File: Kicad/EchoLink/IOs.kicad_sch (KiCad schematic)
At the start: 5 parts, among them J3 Conn_01x08_Pin, J4 Conn_01x06_Pin, J5 Conn_01x09_Socket

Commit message: wip: add comments in schematic
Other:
- note added: "*IMPORTANT STLinkV2 fourni seulement 100-250mA Debogguer avec alimentation 3v3/5v externe"
- moved on the sheet: D2, R15
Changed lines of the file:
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@@
 	(rectangle
 		(start 15.24 85.09)
-		(end 59.69 111.76)
+		(end 61.595 118.745)
 		(stroke
 			(width 0)
@@
 		)
 	)
+	(text "*IMPORTANT\nSTLinkV2 fourni seulement 100-250mA\nDebogguer avec alimentation 3v3/5v externe"
+		(exclude_from_sim no)
+		(at 15.494 115.57 0)
+		(effects
+			(font
+				(size 1.27 1.27)
+				(thickness 0.254)
+				(bold yes)
+				(italic yes)
+			)
+			(justify left)
+		)
+	)
 	(text "HAL_LPTIM_PWM_Start(&hlptim2, 31999, 28799)\nPériode 1s / Flash 100ms\nILED = (3.3 - 2.1) / 1500 = 0.8mA"
 		(exclude_from_sim no)
@@
 	(wire
 		(pts
-			(xy 44.45 71.12) (xy 45.72 71.12)
+			(xy 48.26 71.12) (xy 49.53 71.12)
 		)
 		(stroke
@@
 	(wire
 		(pts
-			(xy 54.61 71.12) (xy 54.61 72.39)
+			(xy 58.42 71.12) (xy 58.42 72.39)
 		)
 		(stroke
@@
 	(wire
 		(pts
-			(xy 35.56 71.12) (xy 36.83 71.12)
-		)
-		(stroke
-			(width 0)
-			(type default)
-		)
-	)
-	(wire
-		(pts
-			(xy 53.34 71.12) (xy 54.61 71.12)
+			(xy 39.37 71.12) (xy 40.64 71.12)
+		)
+		(stroke
+			(width 0)
+			(type default)
+		)
+	)
+	(wire
+		(pts
+			(xy 57.15 71.12) (xy 58.42 71.12)
 		)
 		(stroke
@@
 	(global_label "PWR_LPTIM2_OUT"
 		(shape input)
-		(at 35.56 71.12 180)
+		(at 39.37 71.12 180)
 		(fields_autoplaced yes)
 		(effects
@@
 		)
 		(property "Intersheetrefs" "${INTERSHEET_REFS}"
-			(at 16.4882 71.12 0)
+			(at 20.2982 71.12 0)
 			(hide yes)
 			(show_name no)
@@
 	(symbol
 		(lib_id "Device:LED")
-		(at 49.53 71.12 180)
+		(at 53.34 71.12 180)
 		(unit 1)
 		(body_style 1)
@@
 		(dnp no)
 		(property "Reference" "D2"
-			(at 48.514 68.834 0)
+			(at 52.324 68.834 0)
 			(show_name no)
 			(do_not_autoplace no)
@@
 		)
 		(property "Value" "GREEN"
-			(at 46.99 73.66 0)
+			(at 50.8 73.66 0)
 			(show_name no)
 			(do_not_autoplace no)
@@
 		)
 		(property "Footprint" "ODB:LED_QBLP601-AG15"
-			(at 49.53 71.12 0)
+			(at 53.34 71.12 0)
 			(hide yes)
 			(show_name no)
@@
 		)
 		(property "Datasheet" "https://www.digikey.ca/en/products/detail/qt-brightek-qtb/QBLP601-AG15/16499667"
-			(at 49.53 71.12 0)
+			(at 53.34 71.12 0)
 			(hide yes)
 			(show_name no)
@@
 		)
 		(property "Description" ""
-			(at 49.53 71.12 0)
+			(at 53.34 71.12 0)
 			(hide yes)
 			(show_name no)
@@
 		)
 		(property "DigiKey_Part_Number" "1516-QBLP601-AG15CT-ND"
-			(at 49.53 71.12 0)
+			(at 53.34 71.12 0)
 			(hide yes)
 			(show_name no)
@@
 		)
 		(property "Purchase-URL" ""
-			(at 49.53 71.12 0)
+			(at 53.34 71.12 0)
 			(hide yes)
 			(show_name no)
@@
 		)
 		(property "Sim.Device" ""
-			(at 49.53 71.12 0)
+			(at 53.34 71.12 0)
 			(hide yes)
 			(show_name no)
@@
 		)
 		(property "Sim.Pins" ""
-			(at 49.53 71.12 0)
+			(at 53.34 71.12 0)
 			(hide yes)
 			(show_name no)
@@
 		)
 		(property "Sim.Type" ""
-			(at 49.53 71.12 0)
+			(at 53.34 71.12 0)
 			(hide yes)
 			(show_name no)
@@
 		)
 		(property "Manufacturer_Part_Number" "QBLP601-AG15"
-			(at 49.53 71.12 0)
+			(at 53.34 71.12 0)
 			(hide yes)
 			(show_name no)
@@
 	(symbol
 		(lib_id "power:GND")
-		(at 54.61 72.39 0)
+		(at 58.42 72.39 0)
 		(unit 1)
 		(body_style 1)
@@
 		(fields_autoplaced yes)
 		(property "Reference" "#PWR045"
-			(at 54.61 78.74 0)
+			(at 58.42 78.74 0)
 			(hide yes)
 			(show_name no)
@@
 		)
 		(property "Value" "GND"
-			(at 54.61 77.47 0)
+			(at 58.42 77.47 0)
 			(hide yes)
 			(show_name no)
@@
 		)
 		(property "Footprint" ""
-			(at 54.61 72.39 0)
+			(at 58.42 72.39 0)
 			(hide yes)
 			(show_name no)
@@
 		)
 		(property "Datasheet" ""
-			(at 54.61 72.39 0)
+			(at 58.42 72.39 0)
 			(hide yes)
 			(show_name no)
@@
 		)
 		(property "Description" ""
-			(at 54.61 72.39 0)
+			(at 58.42 72.39 0)
 			(hide yes)
 			(show_name no)
@@
 	(symbol
 		(lib_id "Device:R")
-		(at 40.64 71.12 90)
+		(at 44.45 71.12 90)
 		(unit 1)
 		(body_style 1)
@@
 		(dnp no)
 		(property "Reference" "R15"
-			(at 39.624 69.088 90)
+			(at 43.434 69.088 90)
 			(show_name no)
 			(do_not_autoplace no)
@@
 		)
 		(property "Value" "1.5k"
-			(at 44.45 69.088 90)
+			(at 48.26 69.088 90)
 			(show_name no)
 			(do_not_autoplace no)
@@
 		)
 		(property "Footprint" "Resistor_SMD:R_0603_1608Metric"
-			(at 40.64 72.898 90)
+			(at 44.45 72.898 90)
 			(hide yes)
 			(show_name no)
@@
 		)
 		(property "Datasheet" "https://www.digikey.ca/en/products/detail/panasonic-electronic-components/ERA-3AEB152V/1465858"
-			(at 40.64 71.12 0)
+			(at 44.45 71.12 0)
 			(hide yes)
 			(show_name no)
@@
 		)
 		(property "Description" "Resistor"
-			(at 40.64 71.12 0)
+			(at 44.45 71.12 0)
 			(hide yes)
 			(show_name no)
@@
 		)
 		(property "DigiKey_Part_Number" "P1.5KDBCT-ND"
-			(at 40.64 71.12 90)
+			(at 44.45 71.12 90)
 			(hide yes)
 			(show_name no)
@@
 		)
 		(property "Purchase-URL" ""
-			(at 40.64 71.12 90)
+			(at 44.45 71.12 90)
 			(hide yes)
 			(show_name no)
@@
 		)
 		(property "Sim.Device" ""
-			(at 40.64 71.12 90)
+			(at 44.45 71.12 90)
 			(hide yes)
 			(show_name no)
@@
 		)
 		(property "Sim.Pins" ""
-			(at 40.64 71.12 90)
+			(at 44.45 71.12 90)
 			(hide yes)
 			(show_name no)
@@
 		)
 		(property "Sim.Type" ""
-			(at 40.64 71.12 90)
+			(at 44.45 71.12 90)
 			(hide yes)
 			(show_name no)
@@
 		)
 		(property "Manufacturer_Part_Number" "ERA-3AEB152V"
-			(at 40.64 71.12 90)
-			(hide yes)
-			(show_name no)
+			(at 44.45 71.12 90)
+			(hide yes)
+			(show_name no)

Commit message: wip: add 470uF cap to lora module decoupling capacitance
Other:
- note added: "*Torsader VCC/GND*"
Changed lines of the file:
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@@
+		)
+	)
+	(text "*Torsader VCC/GND*"
+		(exclude_from_sim no)
+		(at 44.45 36.068 0)
+		(effects
+			(font
+				(size 1.27 1.27)
+				(thickness 0.254)
+				(bold yes)
+				(italic yes)
+			)
+			(justify left)
 		)
 	)

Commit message: wip: rename compoents
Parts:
- D2: footprint ODB:LED_QBLP601-AG15 -> (none)
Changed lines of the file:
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@@
 			)
 		)
-		(property "Footprint" "ODB:LED_QBLP601-AG15"
+		(property "Footprint" ""
 			(at 53.34 71.12 0)
 			(hide yes)

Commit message: wip: connector and bms IOs
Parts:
- removed J3: Conn_01x08_Pin, symbol Connector:Conn_01x08_Pin
- removed J5: Conn_01x09_Socket, symbol Connector:Conn_01x09_Socket
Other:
- moved on the sheet: D2, J4, R15

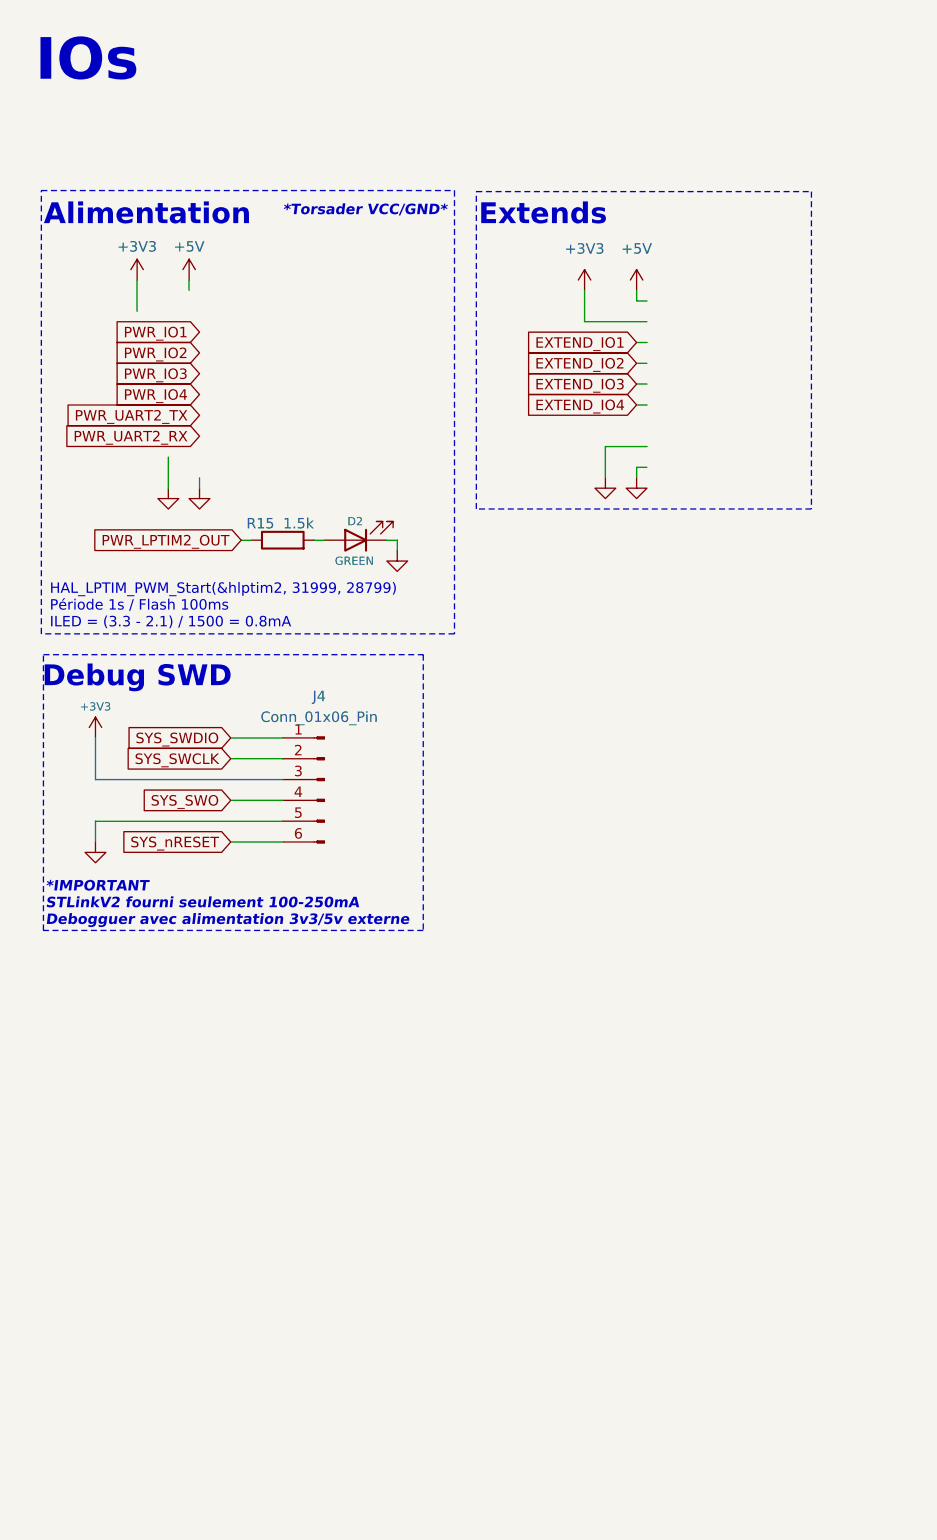
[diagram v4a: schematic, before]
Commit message: fix: rework all schematics to fit with new design and update stm32cubemx project
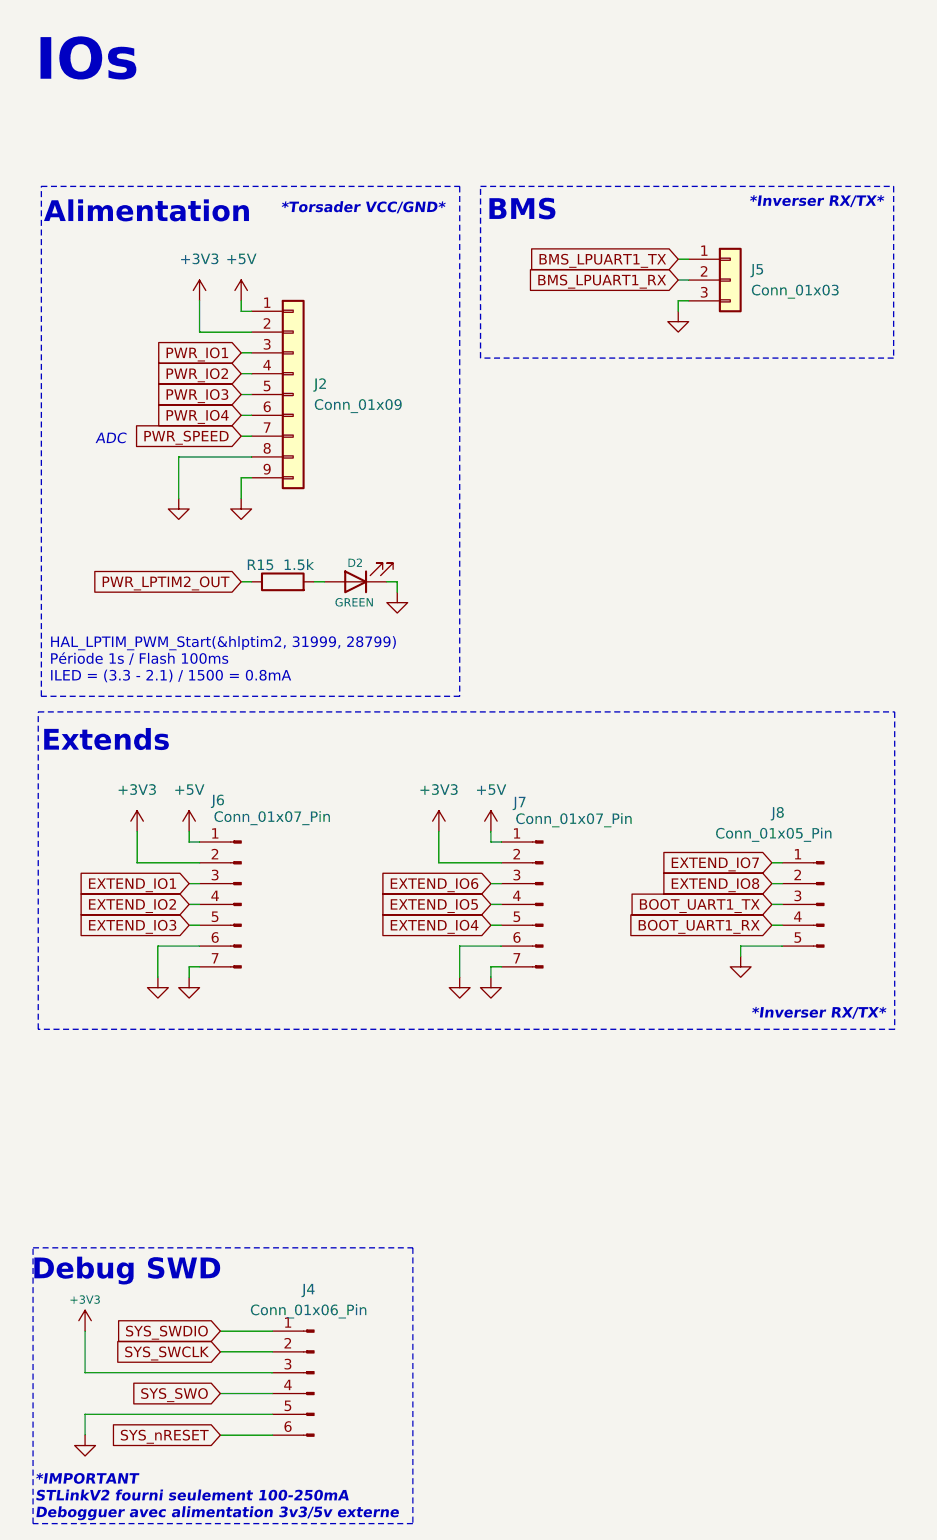
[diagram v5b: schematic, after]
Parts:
- added J2: Conn_01x09, symbol Connector_Generic:Conn_01x09
- added J5: Conn_01x03, Connector_RJ:RJ45_Abracon_ARJP11A-MA_Horizontal, symbol Connector_Generic:Conn_01x03
- added J6, J7: Conn_01x07_Pin, symbol Connector:Conn_01x07_Pin
- added J8: Conn_01x05_Pin, symbol Connector:Conn_01x05_Pin
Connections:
- net +3V3: now also J2.2 (Pin_2), J6.2 (Pin_2), J7.2 (Pin_2)
- net +5V: now also J2.1 (Pin_1), J6.1 (Pin_1), J7.1 (Pin_1)
- net EXTEND_IO1: now also J6.3 (Pin_3)
- net EXTEND_IO2: now also J6.4 (Pin_4)
- net EXTEND_IO3: now also J6.5 (Pin_5)
- net EXTEND_IO4: now also J7.5 (Pin_5)
- net GND: now also J2.8 (Pin_8), J2.9 (Pin_9), J5.3 (Pin_3), J6.6 (Pin_6), J6.7 (Pin_7), J7.6 (Pin_6), J7.7 (Pin_7), J8.5 (Pin_5)
- net PWR_IO1: now also J2.3 (Pin_3)
- net PWR_IO2: now also J2.4 (Pin_4)
- net PWR_IO3: now also J2.5 (Pin_5)
- net PWR_IO4: now also J2.6 (Pin_6)
- new net BMS_LPUART1_RX: J5.2 (Pin_2)
- new net BMS_LPUART1_TX: J5.1 (Pin_1)
- new net BOOT_UART1_RX: J8.4 (Pin_4)
- new net BOOT_UART1_TX: J8.3 (Pin_3)
- new net EXTEND_IO5: J7.4 (Pin_4)
- new net EXTEND_IO6: J7.3 (Pin_3)
- new net EXTEND_IO7: J8.1 (Pin_1)
- new net EXTEND_IO8: J8.2 (Pin_2)
- new net PWR_SPEED: J2.7 (Pin_7)
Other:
- note added: "*Inverser RX/TX*"
- note added: "ADC"
- note added: "BMS"
- moved on the sheet: D2, J4, R15

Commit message: wip: add missing footprints
- connectors missing
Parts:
- D2: footprint (none) -> Resistor_SMD:R_0603_1608Metric
- J3: renamed from J6; footprint (none) -> Connector_PinHeader_2.54mm:PinHeader_1x07_P2.54mm_Vertical
- J5: renamed from J7; footprint (none) -> Connector_PinHeader_2.54mm:PinHeader_1x07_P2.54mm_Vertical
- J6: renamed from J5; footprint Connector_RJ:RJ45_Abracon_ARJP11A-MA_Horizontal -> (none)
- J8: footprint (none) -> Connector_PinHeader_2.54mm:PinHeader_1x05_P2.54mm_Vertical
- renumbered J2 to J4, J4 to J7, R15 to R17
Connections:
- net BOOT_UART1_RX renamed EXTEND_UART1_RX
- net BOOT_UART1_TX renamed EXTEND_UART1_TX
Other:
- moved on the sheet: J7

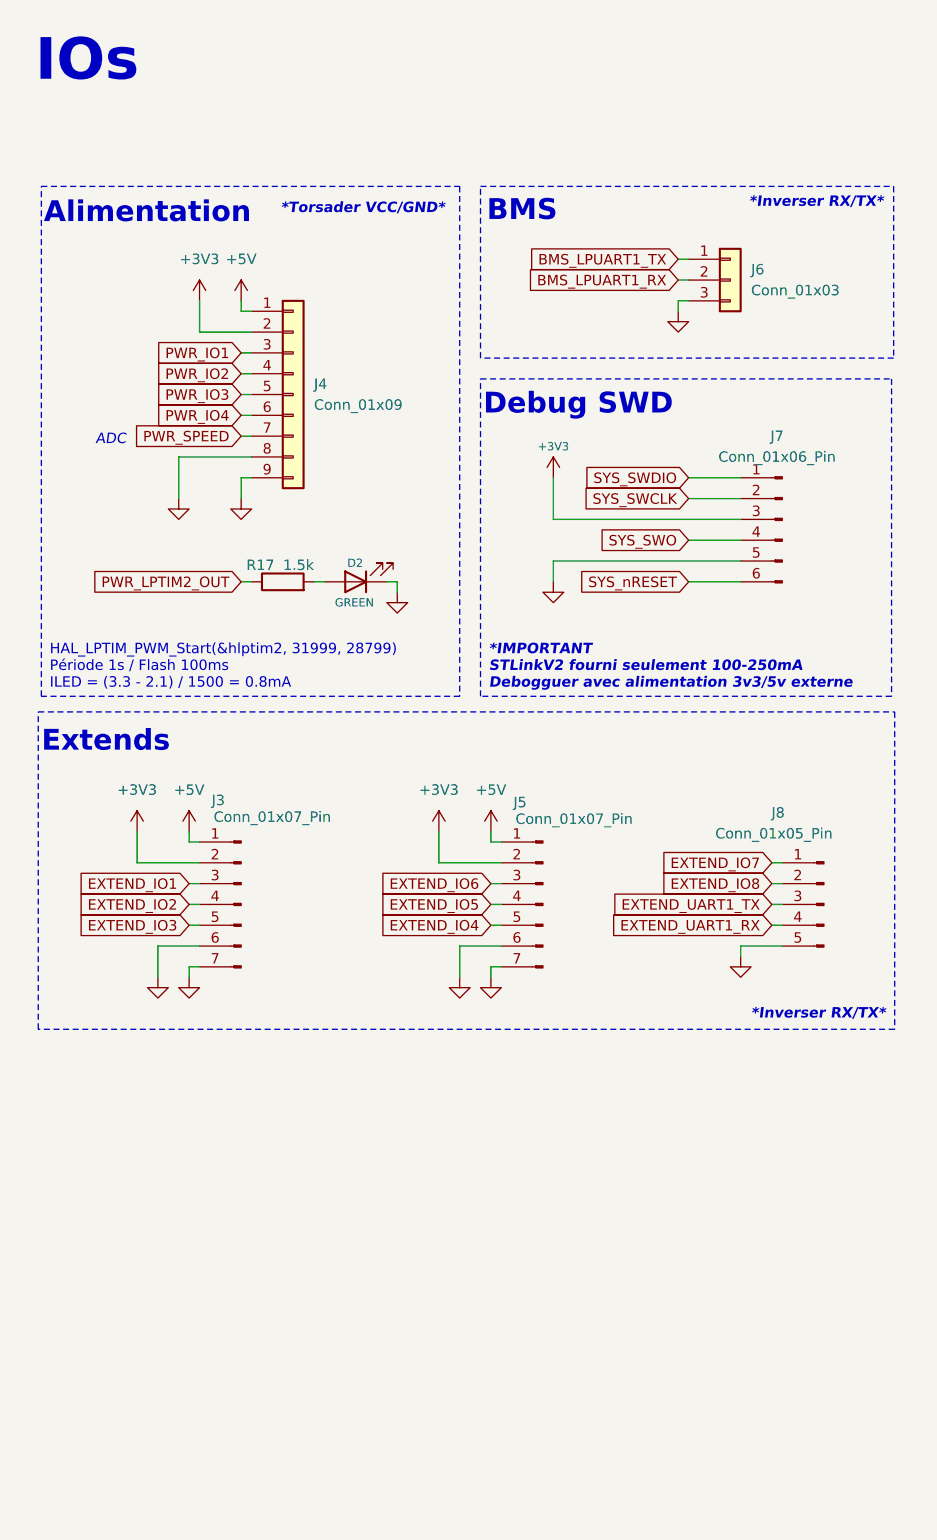
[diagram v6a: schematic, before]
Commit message: wip: add hse crystal and update stm32 project (clock 80MHz and 500kbps CAN)
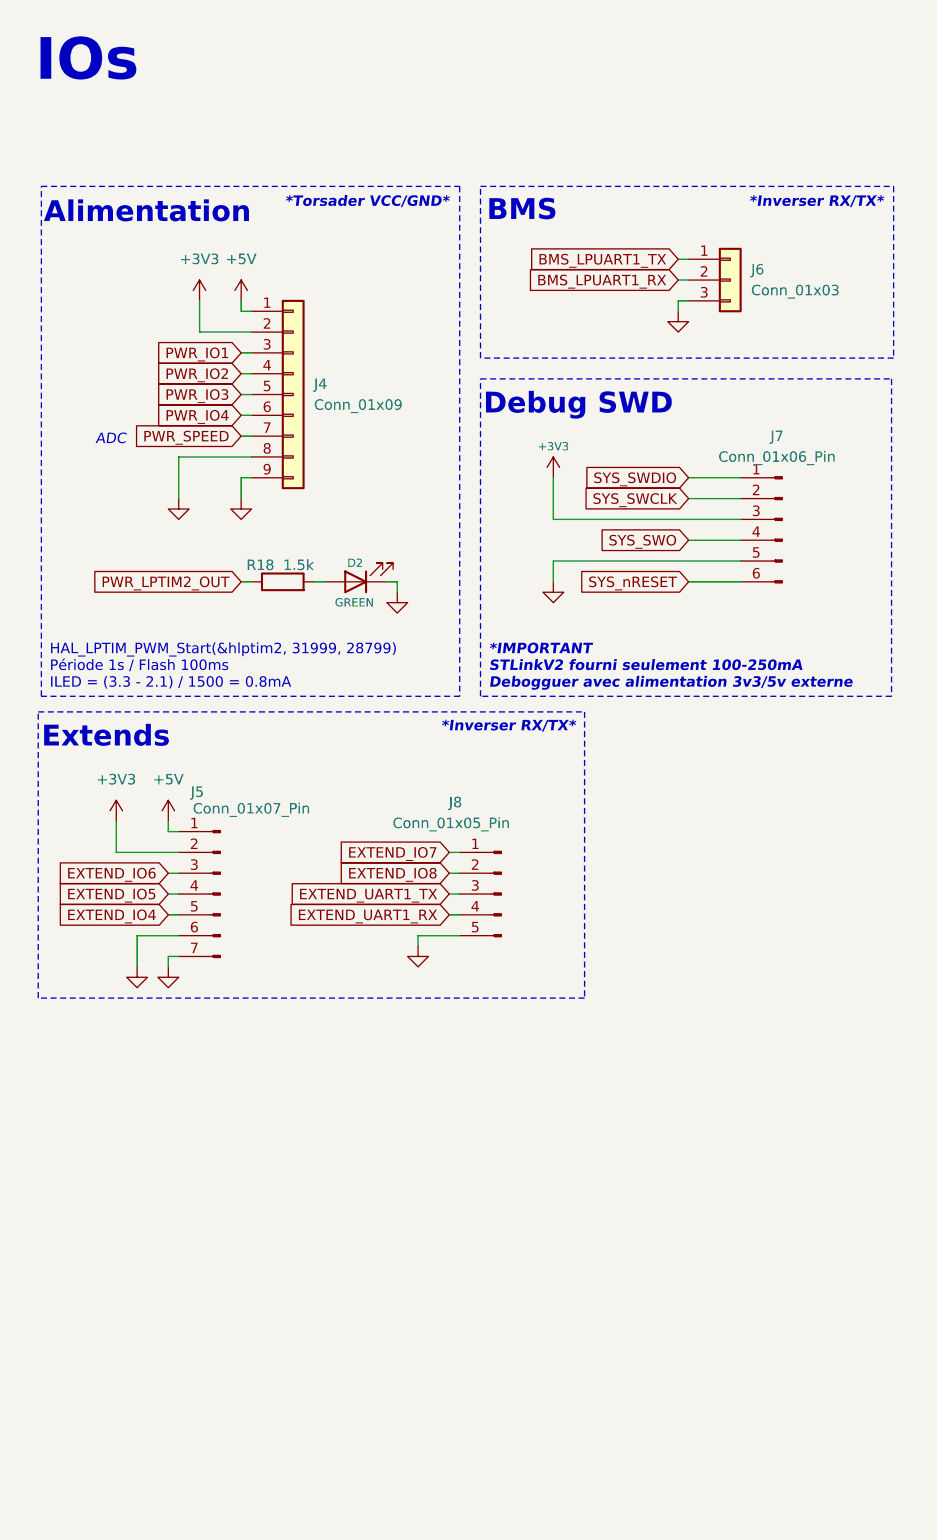
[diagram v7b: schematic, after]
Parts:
- removed J3: Conn_01x07_Pin, Connector_PinHeader_2.54mm:PinHeader_1x07_P2.54mm_Vertical, symbol Connector:Conn_01x07_Pin
- renumbered R17 to R18
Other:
- moved on the sheet: J5, J8
